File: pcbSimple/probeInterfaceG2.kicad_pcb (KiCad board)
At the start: 2 copper layers, 38.1 x 78.7 mm, 20 parts, among them J1 Conn_01x20_Female, J2 Conn_01x20_Female, J3 Conn_02x05_Odd_Even, J4 Conn_01x20_Female, J5 Conn_01x20_Female, U1 SN74AVC4T774GUX

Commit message: cleaned repo and added labels to pcbSimple
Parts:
- moved H3 5.08 mm to (86.4, 124.5)
- moved H4 5.08 mm to (114.3, 124.5)
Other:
- board size 38.1 x 78.7 mm -> 38.1 x 83.8 mm
- board text added: "< GND"
- board text added: "GP0 >"
- board text added: "GP1 >"
- board text added: "GP2 >"
- board text added: "GP3 >"
- board text added: "Vdd >"
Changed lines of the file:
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@@
   )
   (footprint "MountingHole:MountingHole_3.2mm_M3_DIN965_Pad" (layer "F.Cu")
-    (at 114.3 119.38)
+    (at 114.3 124.46)
     (descr "Mounting Hole 3.2mm, M3, DIN965")
     (tags "mounting hole 3.2mm m3 din965")
@@
   )
   (footprint "MountingHole:MountingHole_3.2mm_M3_DIN965_Pad" (layer "F.Cu")
-    (at 86.36 119.38)
+    (at 86.36 124.46)
     (descr "Mounting Hole 3.2mm, M3, DIN965")
     (tags "mounting hole 3.2mm m3 din965")
@@
     )
   )
-  (gr_line (start 119.38 124.46) (end 119.38 45.72) (layer "Edge.Cuts") (width 0.1))
-  (gr_line (start 81.28 45.72) (end 81.28 124.46) (layer "Edge.Cuts") (width 0.1))
+  (gr_line (start 119.38 129.54) (end 119.38 45.72) (layer "Edge.Cuts") (width 0.1))
+  (gr_line (start 81.28 45.72) (end 81.28 129.54) (layer "Edge.Cuts") (width 0.1))
   (gr_line (start 119.38 45.72) (end 81.28 45.72) (layer "Edge.Cuts") (width 0.1))
-  (gr_line (start 81.28 124.46) (end 119.38 124.46) (layer "Edge.Cuts") (width 0.1))
+  (gr_line (start 81.28 129.54) (end 119.38 129.54) (layer "Edge.Cuts") (width 0.1))
+  (gr_text "GP0 >" (at 104.14 123.825 90) (layer "F.SilkS")
+    (effects (font (size 1 1) (thickness 0.15)))
+  )
+  (gr_text "GP1 >" (at 101.6 123.825 90) (layer "F.SilkS")
+    (effects (font (size 1 1) (thickness 0.15)))
+  )
+  (gr_text "Vdd >" (at 93.98 123.825 90) (layer "F.SilkS")
+    (effects (font (size 1 1) (thickness 0.15)))
+  )
+  (gr_text "GP3 >" (at 96.52 123.825 90) (layer "F.SilkS")
+    (effects (font (size 1 1) (thickness 0.15)))
+  )
+  (gr_text "GP2 >" (at 99.06 123.825 90) (layer "F.SilkS")
+    (effects (font (size 1 1) (thickness 0.15)))
+  )
+  (gr_text "< GND" (at 108.585 116.84) (layer "F.SilkS")
+    (effects (font (size 1 1) (thickness 0.15)))
+  )
   (segment (start 100.93 106.08) (end 102.87 104.14) (width 0.22) (layer "F.Cu") (net 1))
   (segment (start 100.93 107.225) (end 100.93 106.08) (width 0.22) (layer "F.Cu") (net 1))
@@
     (polygon
       (pts
-        (xy 119.38 124.46)
-        (xy 81.28 124.46)
+        (xy 119.38 129.54)
+        (xy 81.28 129.54)
         (xy 81.28 45.72)
         (xy 119.38 45.72)

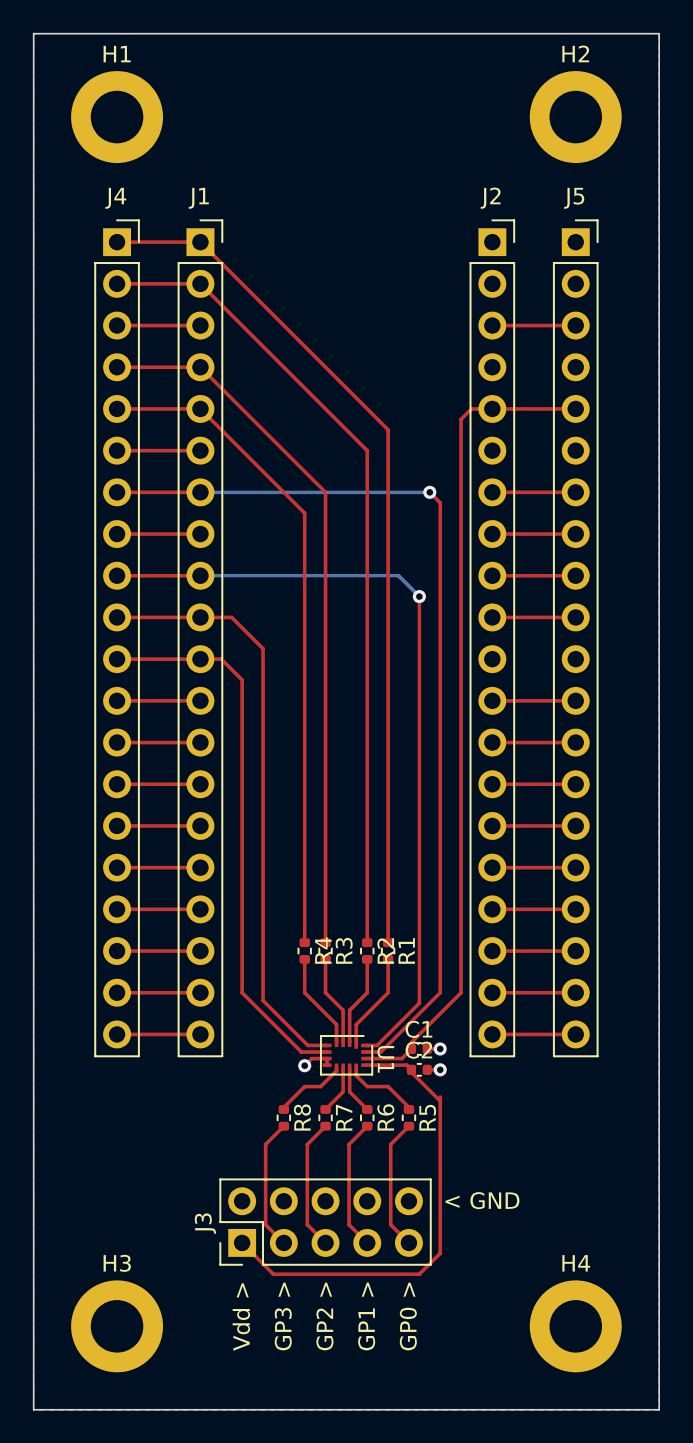
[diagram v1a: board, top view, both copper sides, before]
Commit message: simplified simplePCB
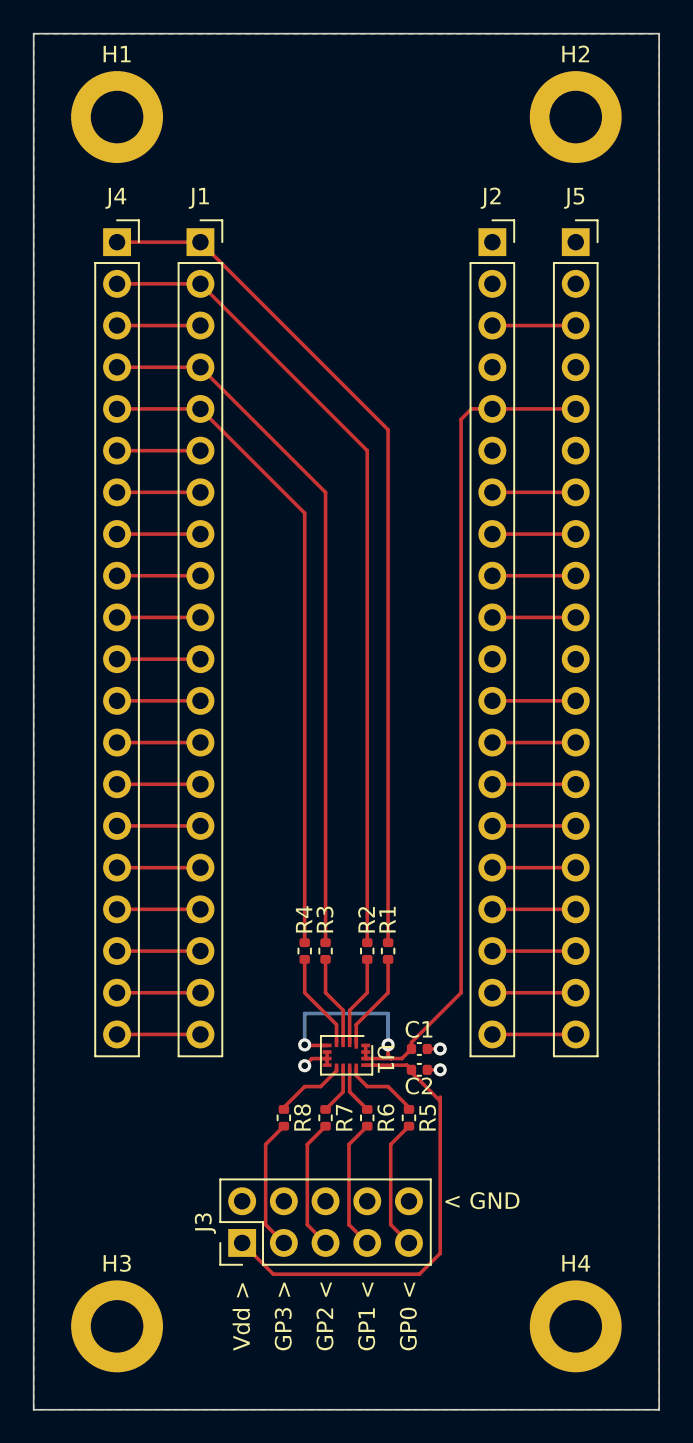
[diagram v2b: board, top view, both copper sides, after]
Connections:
- U1 pad 15: /GP5 -> +3V3
- U1 pad 16: /GP6 -> +3V3
- U1 pad 5: /GP7 -> +3V3
- U1 pad 6: /GP8 -> GND
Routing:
- net /GP5: track 55.8 -> 5.08 mm, vias 1 -> 0
- net /GP6: track 48.0 -> 5.08 mm, vias 1 -> 0
- net /GP7: track 36.1 -> 5.08 mm
- net /GP8: track 33.9 -> 5.08 mm
- net +3V3: track 49.9 -> 61.9 mm, vias 0 -> 2
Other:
- board text added: "GP0 <"
- board text added: "GP1 <"
- board text added: "GP2 <"
- board text removed: "GP0 >"
- board text removed: "GP1 >"
- board text removed: "GP2 >"
